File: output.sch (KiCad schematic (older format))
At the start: 7 parts, among them J1 5-20 V⎓, Q1 MMBT2222ALT1G, Q2 DMP4015SSS

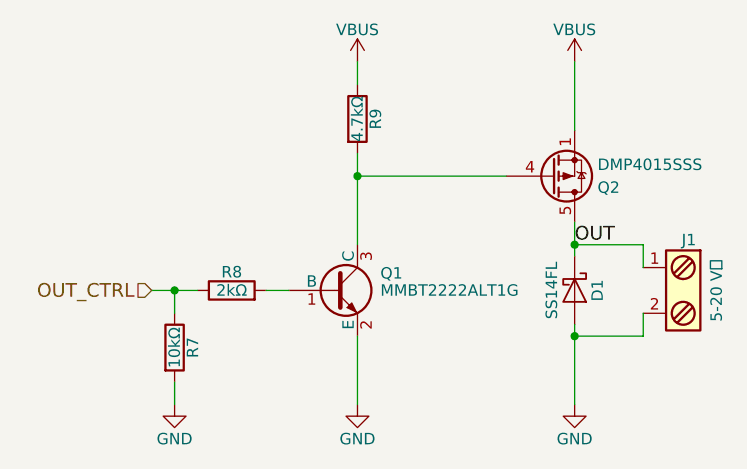
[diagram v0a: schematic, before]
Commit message: Changed R9 to 100 kΩ
As it was, it wasted around 85 mW whenever the output was turned on at
20 V.  That's a silly waste of power.  A 100 kΩ pullup works just fine,
so I changed it.  Now there's only 4 mW wasted, so I'm happy.
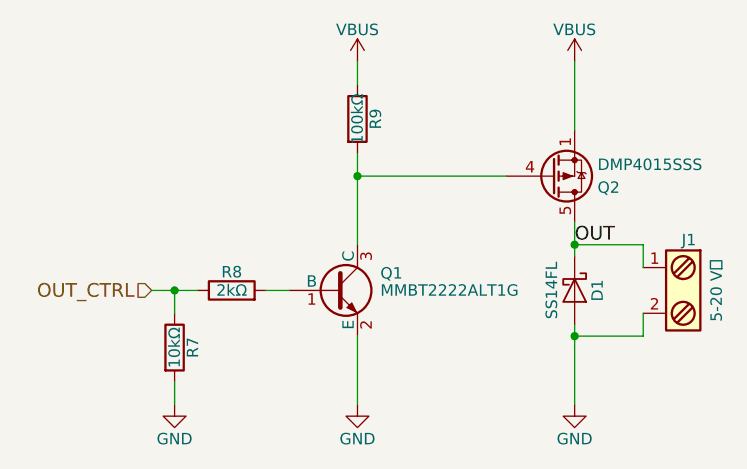
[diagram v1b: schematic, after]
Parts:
- R9: value 4.7kΩ -> 100kΩ
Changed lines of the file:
@@
 P 5550 3300
 F 0 "R9" V 5630 3300 50  0000 C CNN
-F 1 "4.7kΩ" V 5550 3300 50  0000 C CNN
+F 1 "100kΩ" V 5550 3300 50  0000 C CNN
 F 2 "Resistors_SMD:R_0805" V 5480 3300 50  0001 C CNN
 F 3 "" H 5550 3300 50  0000 C CNN

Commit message: 4-layer board with smaller components
This is a major change!  Almost all the components have changed to
smaller versions, with 0603 and 0402 passives and a QFN microcontroller.
The board now has four layers, with internal layers used for VBUS and
GND.  The board now measures a mere 25×30 mm!  The SWD header and Boot
switch footprints have been moved to the bottom to help with this
shrinkage.  Two test points were added to the bottom as well to make it
possible to power the board without using the USB connector.  The
mounting holes are now slightly smaller (better sized for M3), and only
17 mm apart instead of the old 18 mm.

To sum up, everything is smaller and that's almost entirely a good
thing, except now it's not really possible to build one by hand.
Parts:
- R7, R8, R9: footprint Resistors_SMD:R_0805 -> Resistors_SMD:R_0402
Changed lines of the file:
@@
 	5150 4050 5250 4050
 $Comp
-L GND #PWR021
+L GND #PWR023
 U 1 1 58925B13
 P 5550 4550
-F 0 "#PWR021" H 5550 4300 50  0001 C CNN
+F 0 "#PWR023" H 5550 4300 50  0001 C CNN
 F 1 "GND" H 5550 4400 50  0000 C CNN
 F 2 "" H 5550 4550 50  0000 C CNN
@@
 	5550 4550 5550 4250
 $Comp
-L GND #PWR022
+L GND #PWR024
 U 1 1 58925CFD
 P 6500 4550
-F 0 "#PWR022" H 6500 4300 50  0001 C CNN
+F 0 "#PWR024" H 6500 4300 50  0001 C CNN
 F 1 "GND" H 6500 4400 50  0000 C CNN
 F 2 "" H 6500 4550 50  0000 C CNN
@@
 	6500 3350 6500 3050
 $Comp
-L VBUS #PWR023
+L VBUS #PWR025
 U 1 1 58925D31
 P 6500 3050
-F 0 "#PWR023" H 6500 2900 50  0001 C CNN
+F 0 "#PWR025" H 6500 2900 50  0001 C CNN
 F 1 "VBUS" H 6500 3190 50  0000 C CNN
 F 2 "" H 6500 3050 50  0000 C CNN
@@
 F 0 "R9" V 5630 3300 50  0000 C CNN
 F 1 "100kΩ" V 5550 3300 50  0000 C CNN
-F 2 "Resistors_SMD:R_0805" V 5480 3300 50  0001 C CNN
+F 2 "Resistors_SMD:R_0402" V 5480 3300 50  0001 C CNN
 F 3 "" H 5550 3300 50  0000 C CNN
 	1    5550 3300
@@
 Connection ~ 5550 3550
 $Comp
-L VBUS #PWR024
+L VBUS #PWR026
 U 1 1 589260BE
 P 5550 3050
-F 0 "#PWR024" H 5550 2900 50  0001 C CNN
+F 0 "#PWR026" H 5550 2900 50  0001 C CNN
 F 1 "VBUS" H 5550 3190 50  0000 C CNN
 F 2 "" H 5550 3050 50  0000 C CNN
@@
 F 0 "R8" V 5080 4050 50  0000 C CNN
 F 1 "2kΩ" V 5000 4050 50  0000 C CNN
-F 2 "Resistors_SMD:R_0805" V 4930 4050 50  0001 C CNN
+F 2 "Resistors_SMD:R_0402" V 4930 4050 50  0001 C CNN
 F 3 "" H 5000 4050 50  0000 C CNN
 	1    5000 4050
@@
 F 0 "R7" V 4830 4300 50  0000 C CNN
 F 1 "10kΩ" V 4750 4300 50  0000 C CNN
-F 2 "Resistors_SMD:R_0805" V 4680 4300 50  0001 C CNN
+F 2 "Resistors_SMD:R_0402" V 4680 4300 50  0001 C CNN
 F 3 "" H 4750 4300 50  0000 C CNN
 	1    4750 4300
@@
 Connection ~ 4750 4050
 $Comp
-L GND #PWR025
+L GND #PWR027
 U 1 1 58926FD3
 P 4750 4550
-F 0 "#PWR025" H 4750 4300 50  0001 C CNN
+F 0 "#PWR027" H 4750 4300 50  0001 C CNN
 F 1 "GND" H 4750 4400 50  0000 C CNN
 F 2 "" H 4750 4550 50  0000 C CNN
